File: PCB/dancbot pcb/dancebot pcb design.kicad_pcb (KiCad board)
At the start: 2 copper layers, 27 parts, among them J1 ESP32-PICO-KIT-V4.1, J2 Voltage Regulator, J4 Pins, J6 Conn_01x04_Socket, J7 Conn_01x04_Socket, Q1 IRLML6402TRPBF, Q2 IRLML2502, Q3 2N3904, Q4 PMOS, SW1 SP switch, SW2 SW_SPST

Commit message: Layout Revision 2
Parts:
- removed Q1: IRLML6402TRPBF, IRLML6402TRPBF:SOT95P237X112-3N
- added Q5: PMOS, dancebot pcb libraries stuff:TO254P1052X465X1989-3, F.Cu at (229.0, 101.0)
- Q2: value IRLML2502 -> PMOS; footprint IRLML2502:SOT95P237X112-3N -> dancebot pcb libraries stuff:TO254P1052X465X1989-3
- moved IO18 54.0 mm to (210.0, 109.0), turned to 180 degrees
- moved Q4 53.7 mm to (238.0, 68.0), turned to 90 degrees
- moved R5 50.6 mm to (232.0, 68.0), turned to 90 degrees
- moved J4 48.9 mm to (200.0, 108.0), turned to 180 degrees
- moved J2 44.0 mm to (196.7, 108.0), turned to 180 degrees
- moved R7 43.7 mm to (225.1, 68.1), turned to -90 degrees
- moved Q3 37.8 mm to (224.7, 62.0), turned to 0 degrees
- moved SW1 34.8 mm to (189.0, 68.0)
- moved R3 34.3 mm to (207.0, 100.1), turned to 90 degrees
- moved R4 31.8 mm to (229.0, 68.1), turned to -90 degrees
- moved BT1 29.8 mm to (192.0, 107.0), turned to 90 degrees
- moved SW2 28.1 mm to (192.0, 102.0), turned to 180 degrees
- moved R2 20.3 mm to (211.0, 100.1), turned to 90 degrees
- moved IO14 20.3 mm to (214.0, 108.9), turned to 180 degrees
- moved R6 18.8 mm to (221.0, 68.0), turned to 90 degrees
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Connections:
- net Latch_in renamed Latch_Out
- BT1 pad 2: Batt GND -> GND1
- IO12 pad 1: +5V -> VOUT
- IO12 pad 2: Batt GND -> GND1
- IO13 pad 1: +5V -> VOUT
- IO13 pad 2: Batt GND -> GND1
- IO14 pad 1: +5V -> VOUT
- IO14 pad 2: Batt GND -> GND1
- IO15 pad 1: +5V -> VOUT
- IO15 pad 2: Batt GND -> GND1
- IO18 pad 1: +5V -> VOUT
- IO18 pad 2: Batt GND -> GND1
- J1 pad J2_19: Batt GND -> GND1
- J1 pad J3_10: unconnected-(J1-IO27-PadJ3_10) -> BATT ADC
- J1 pad J3_16: unconnected-(J1-IO4-PadJ3_16) -> BATT EN
- J2 pad 1: +5V -> VOUT
- J2 pad 2: Batt GND -> GND1
- J4 pad 1: Batt GND -> GND1
- J6 pad 2: Batt GND -> GND1
- J7 pad 2: Batt GND -> GND1
- Q2 pad 1: Batt PWR -> Net-(Q2-D)
- Q2 pad 2: Batt GND -> BATT EN
- Q2 pad 3: Net-(Q1-Pad1) -> GND1
- Q3 pad 1: Batt GND -> GND1
- Q3 pad 2: Net-(D1-A) -> Net-(D1-K)
- R1 pad 1: +5V -> VOUT
- R1 pad 2: Net-(Q1-Pad1) -> Net-(Q2-D)
- R2 pad 2: BAT_ADC -> BATT ADC
- R3 pad 1: BAT_ADC -> BATT ADC
- R3 pad 2: Batt GND -> GND1
- R4 pad 2: Batt GND -> GND1
- R6 pad 2: Net-(D1-K) -> Net-(D1-A)
- R7 pad 1: Net-(D1-A) -> Net-(D1-K)
- R7 pad 2: Batt GND -> GND1
- R8 pad 1: Net-(D1-A) -> Net-(D1-K)
- SW2 pad 1: Net-(BT1-+) -> VOUT
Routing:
- net Batt GND: track 193.3 -> 0.00 mm
- net +5V: track 178.2 -> 0.00 mm, vias 6 -> 0
- net Net-(D1-A): track 51.3 -> 0.00 mm
- net Net-(R4-Pad1): track 39.9 -> 0.00 mm
- net SM5: track 33.8 -> 0.00 mm
- net NPLeftEye: track 31.0 -> 0.00 mm
- net Net-(Q4-G): track 28.1 -> 0.00 mm
- net Batt PWR: track 23.8 -> 0.00 mm
- net SM1: track 17.1 -> 0.00 mm
- net BAT_ADC: track 14.8 -> 0.00 mm
- net NPRightEye: track 14.1 -> 0.00 mm
- net Latch_Out: track 12.3 -> 0.00 mm
- net Net-(Q1-Pad1): track 11.9 -> 0.00 mm
- net Net-(Q5-S): track 11.6 -> 0.00 mm
- net SM4: track 9.54 -> 0.00 mm
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- added copper zone on F.Cu, net GND1

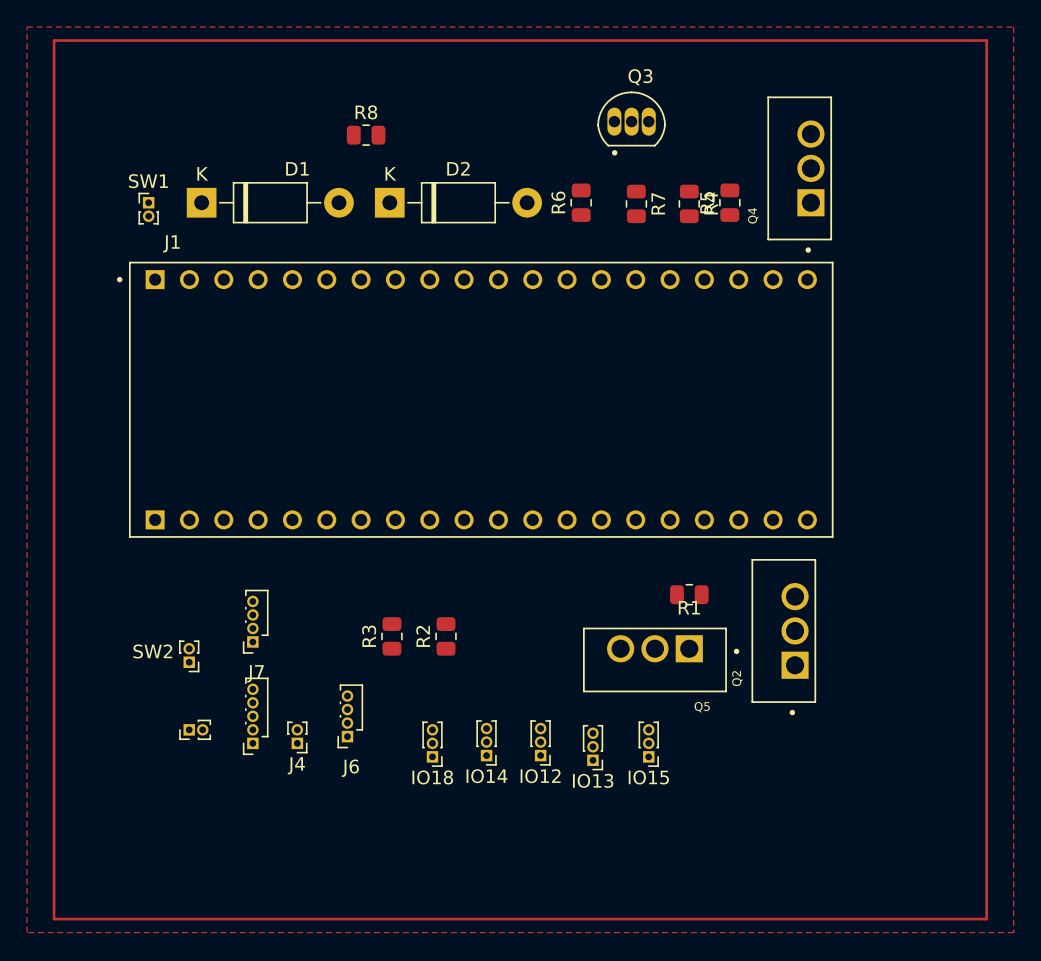
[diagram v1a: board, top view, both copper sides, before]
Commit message: Connections For Layout Revision 1
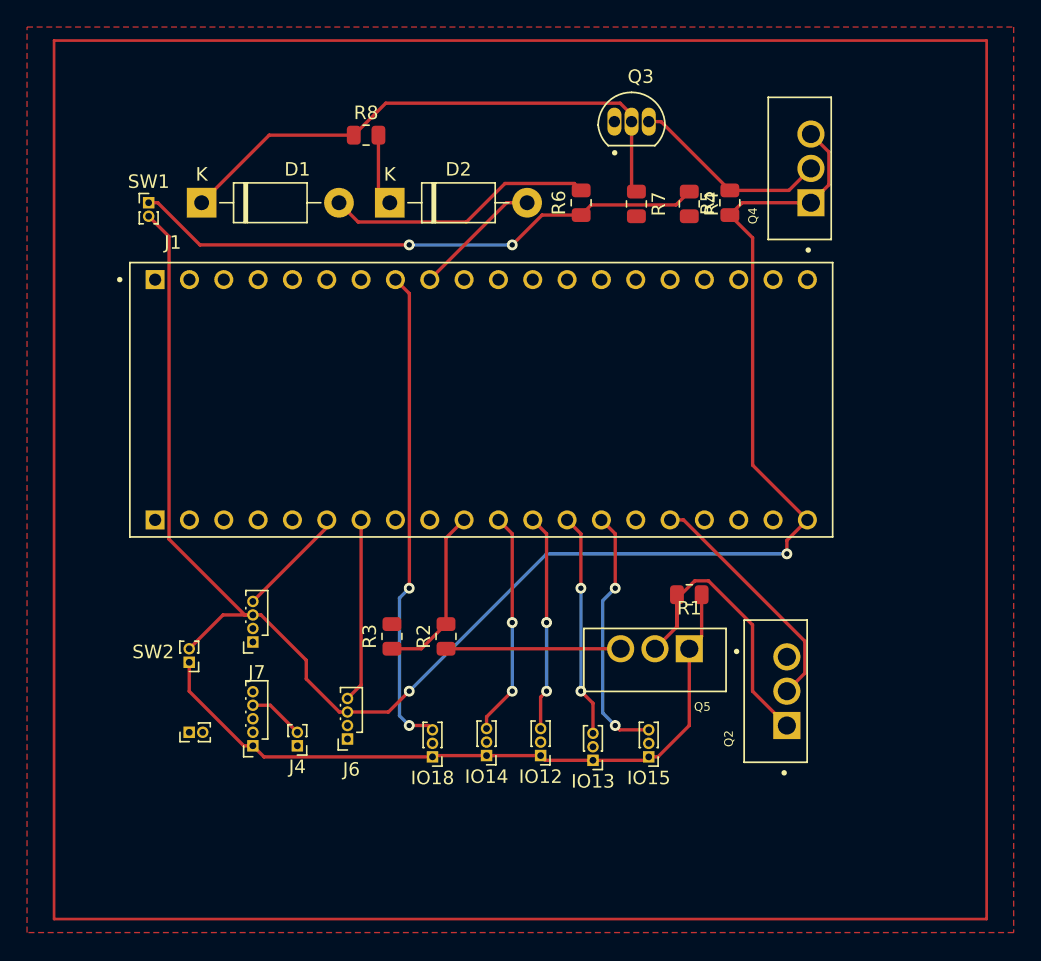
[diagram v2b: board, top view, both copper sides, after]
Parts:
- moved Q2 4.50 mm to (236.2, 106.7)
- moved BT1 0.18 mm to (192.0, 107.2)
- moved J2 0.18 mm to (196.7, 108.2)
- moved J4 0.18 mm to (200.0, 108.2)
- moved J6 0.18 mm to (203.7, 107.7)
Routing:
- net +5V: track 0.00 -> 127.6 mm, vias 0 -> 2
- net VOUT: track 0.00 -> 52.5 mm
- net Net-(R4-Pad1): track 0.00 -> 42.9 mm, vias 0 -> 2
- net Net-(D1-K): track 0.00 -> 41.1 mm
- net SM5: track 0.00 -> 35.9 mm, vias 0 -> 2
- net Net-(Q2-D): track 0.00 -> 22.7 mm
- net Net-(D1-A): track 0.00 -> 19.9 mm
- net SM4: track 0.00 -> 19.0 mm, vias 0 -> 2
- net BATT EN: track 0.00 -> 17.9 mm
- net SM1: track 0.00 -> 16.6 mm, vias 0 -> 2
- net SM3: track 0.00 -> 16.6 mm, vias 0 -> 2
- net SM2: track 0.00 -> 16.0 mm, vias 0 -> 2
- net Net-(Q4-G): track 0.00 -> 14.8 mm
- net NPRightEye: track 0.00 -> 13.6 mm
- net BATT ADC: track 0.00 -> 13.0 mm
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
